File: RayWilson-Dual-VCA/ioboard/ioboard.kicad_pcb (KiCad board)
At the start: 2 copper layers, 108 x 71.8 mm, 90 parts, among them IC1 TL074P, IC2 LM13700N, Q1 2N3904, Q2 2N3906, Q3 2N3904, Q4 2N3906

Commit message: Update ioboard
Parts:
- removed @HOLE0, @HOLE1, @HOLE10, @HOLE2, @HOLE3, @HOLE4, @HOLE5, @HOLE6, @HOLE7, @HOLE8, @HOLE9: , 
- AUDIO_IN_1, AUDIO_IN_2, AUDIO_OUT_1, AUDIO_OUT_2, CV1_1, CV1_2, CV2_1, CV2_2: value PJ301BMPJ301BM -> AudioJack2_SwitchT; footprint ioboard:PJ301BM -> Connector_Audio:Jack_3.5mm_QingPu_WQP-PJ398SM_Vertical_CircularHoles
- JP1, JP2, JP3, JP4: value (none) -> PINHD-1X6
- JP5, JP6: value (none) -> PINHD-1X4
- PWR0: value (none) -> ML10
- S1, S2: value (none) -> M9040P
- moved CV2_2 6.49 mm to (163.1, 126.8), turned to 0 degrees
- moved CV1_2 6.48 mm to (194.8, 126.8), turned to 0 degrees
- moved AUDIO_IN_2 6.47 mm to (113.6, 126.8), turned to 0 degrees
- moved CV1_1 6.47 mm to (194.8, 119.4), turned to 180 degrees
- moved CV2_1 6.47 mm to (163.1, 119.4), turned to 180 degrees
- moved AUDIO_OUT_2 6.46 mm to (100.9, 126.8), turned to 0 degrees
- moved AUDIO_OUT_1 6.46 mm to (100.9, 119.4), turned to 180 degrees
- moved AUDIO_IN_1 6.45 mm to (113.6, 119.4), turned to 180 degrees
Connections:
- net AI1_M renamed /AI1_M
- net AI2_M renamed /AI2_M
- net AO1_M renamed /AO1_M
- net AO2_M renamed /AO2_M
- net CV1_IO renamed /CV1_IO
- net CV1_M renamed /CV1_M
- net CV2_IO renamed /CV2_IO
- net CV2_M renamed /CV2_M
- net IO_CV1 renamed Net-(CV_ATTN_1-Pad1)
- net IO_CV2 renamed Net-(CV_ATTN_2-Pad1)
- net SWA1_IO renamed /SWA1_IO
- net SWA1_M renamed /SWA1_M
- net SWA2_IO renamed /SWA2_IO
- net SWA2_M renamed /SWA2_M
- net SWB1_IO renamed /SWB1_IO
- net SWB1_M renamed /SWB1_M
- net SWB2_IO renamed /SWB2_IO
- net SWB2_M renamed /SWB2_M
- net SWC1_IO renamed /SWC1_IO
- net SWC1_M renamed /SWC1_M
- net SWC2_IO renamed /SWC2_IO
- net SWC2_M renamed /SWC2_M
- CV_ATTN_1 pad 2: N$41 -> Net-(CV1_1-PadT)
- CV_ATTN_2 pad 2: N$46 -> Net-(CV1_2-PadT)
- IC2 pad 15: (no net) -> unconnected-(IC2-Pad15)
- IC2 pad 2: (no net) -> unconnected-(IC2-Pad2)
- JP1 pad 2: AI2_IO -> /AI2_IO
- JP1 pad 6: AO2_IO -> /AO2_IO
- JP2 pad 2: AI1_IO -> /AI1_IO
- JP2 pad 6: AO1_IO -> /AO1_IO
- R1 pad S@1: (no net) -> unconnected-(R1-PadS@1)
- R16 pad 1: N$12 -> Net-(CV2_1-PadT)
- R2 pad S@1: (no net) -> unconnected-(R2-PadS@1)
- R3 pad S@1: (no net) -> unconnected-(R3-PadS@1)
- R36 pad 1: N$48 -> Net-(CV2_2-PadT)
- R4 pad S@1: (no net) -> unconnected-(R4-PadS@1)
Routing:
- net /AO1_IO: track 0.00 -> 30.6 mm
- net /AO2_IO: track 0.00 -> 30.2 mm
- net N$46: track 29.1 -> 0.00 mm
- net N$41: track 29.1 -> 0.00 mm
- net /AI2_IO: track 0.00 -> 28.7 mm
- net AI2_IO: track 27.5 -> 0.00 mm
- net /AI1_IO: track 0.00 -> 26.3 mm
- net Net-(CV1_2-PadT): track 0.00 -> 24.3 mm
- net Net-(CV1_1-PadT): track 0.00 -> 24.3 mm
- net AO1_IO: track 23.7 -> 0.00 mm
- net AO2_IO: track 22.9 -> 0.00 mm
- net AI1_IO: track 19.5 -> 0.00 mm
- net N$12: track 15.7 -> 0.00 mm
- net N$48: track 14.7 -> 0.00 mm
- net Net-(CV2_1-PadT): track 0.00 -> 9.88 mm
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
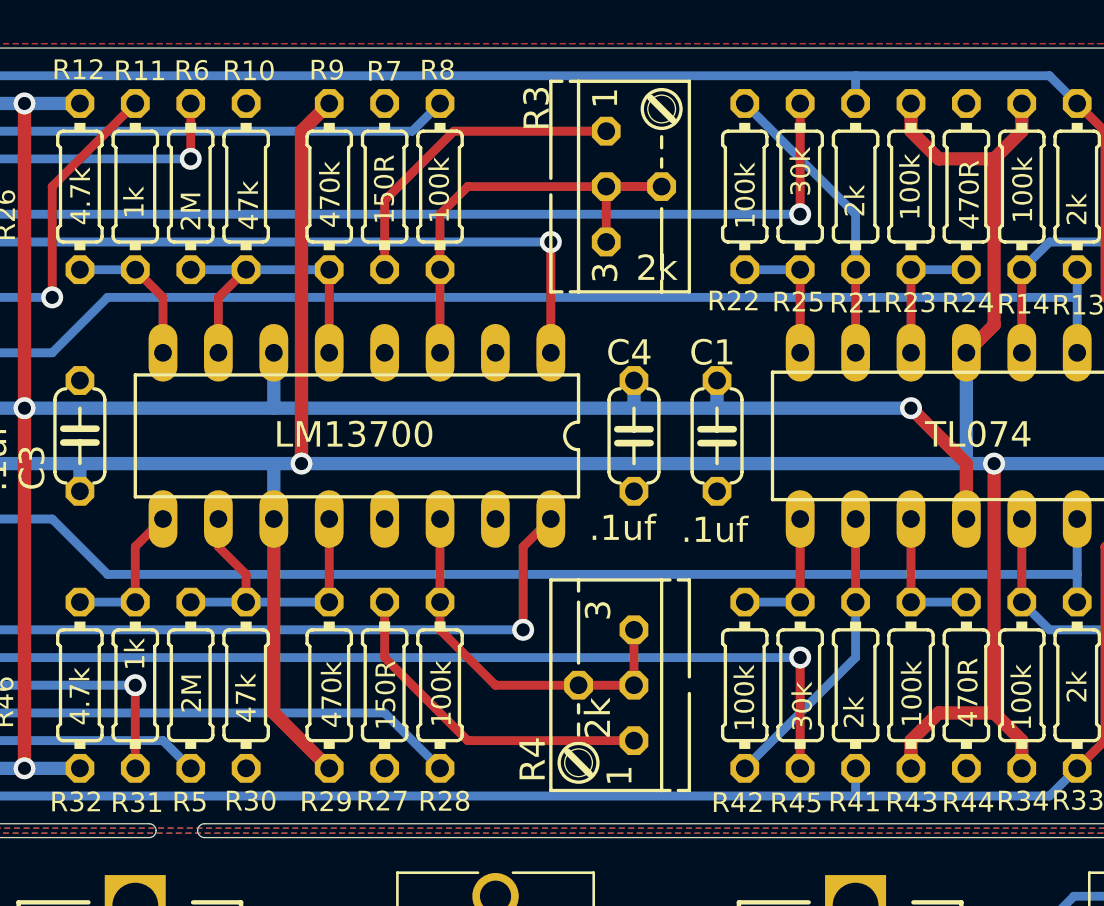
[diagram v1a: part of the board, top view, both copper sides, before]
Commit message: Change LM13700 to be SMD since that's the only part available
In both TME and LCSC.
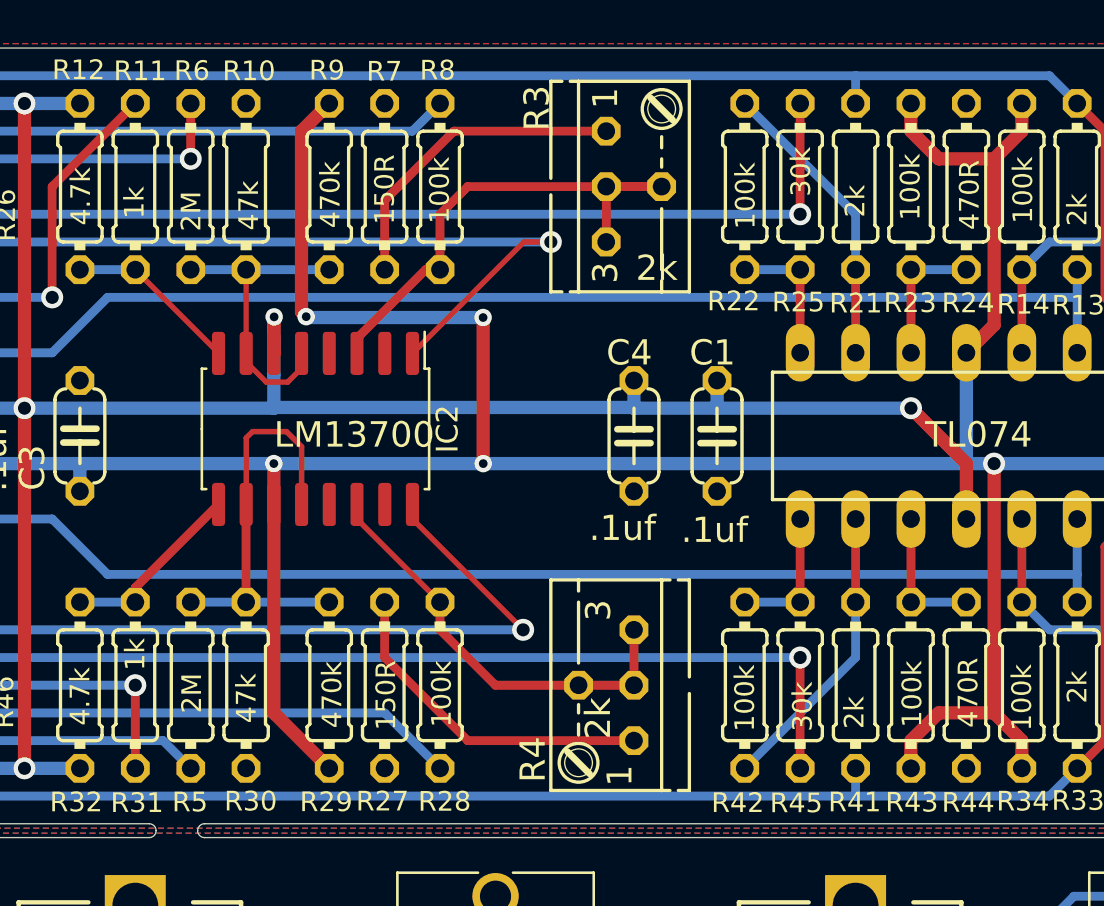
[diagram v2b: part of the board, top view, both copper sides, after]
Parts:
- IC2: footprint ioboard:DIL16 -> Package_SO:SO-16_5.3x10.2mm_P1.27mm
- moved IC2 1.93 mm to (154.9, 86.6), turned to -90 degrees
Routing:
- net +12V: track 275.8 -> 283.9 mm, vias 2 -> 5
- net Net-(IC2-Pad10): track 14.5 -> 19.5 mm
- net /SWB1_M: track 48.3 -> 51.6 mm
- net -12V: track 212.1 -> 215.4 mm, vias 5 -> 6
- net /SWB2_M: track 47.5 -> 49.8 mm
- net Net-(IC2-Pad14): track 17.6 -> 19.8 mm
- net Net-(IC2-Pad3): track 22.1 -> 24.1 mm
- net Net-(IC2-Pad9): track 6.88 -> 8.60 mm
- net Net-(IC2-Pad8): track 6.88 -> 7.96 mm

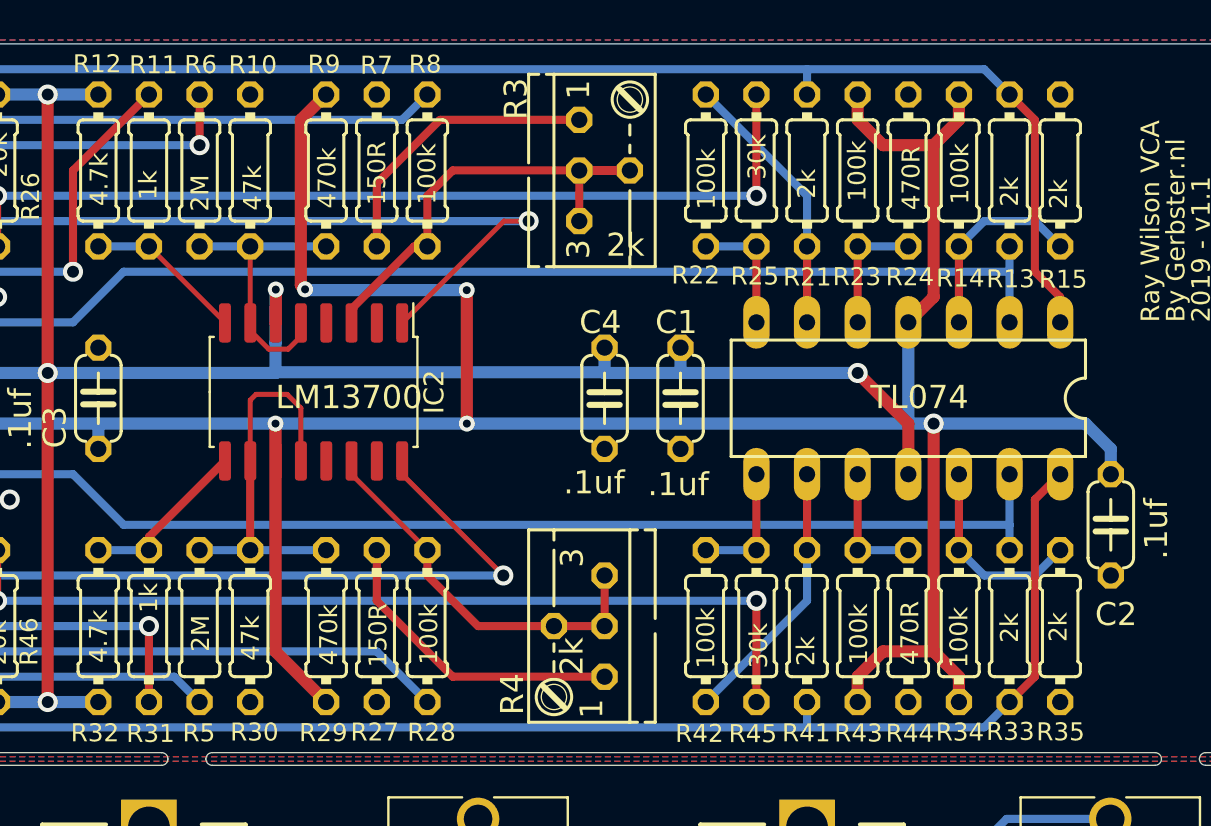
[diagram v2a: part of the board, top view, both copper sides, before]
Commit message: Replace TL047P with SMD
Since that's the only package available from LCSC.
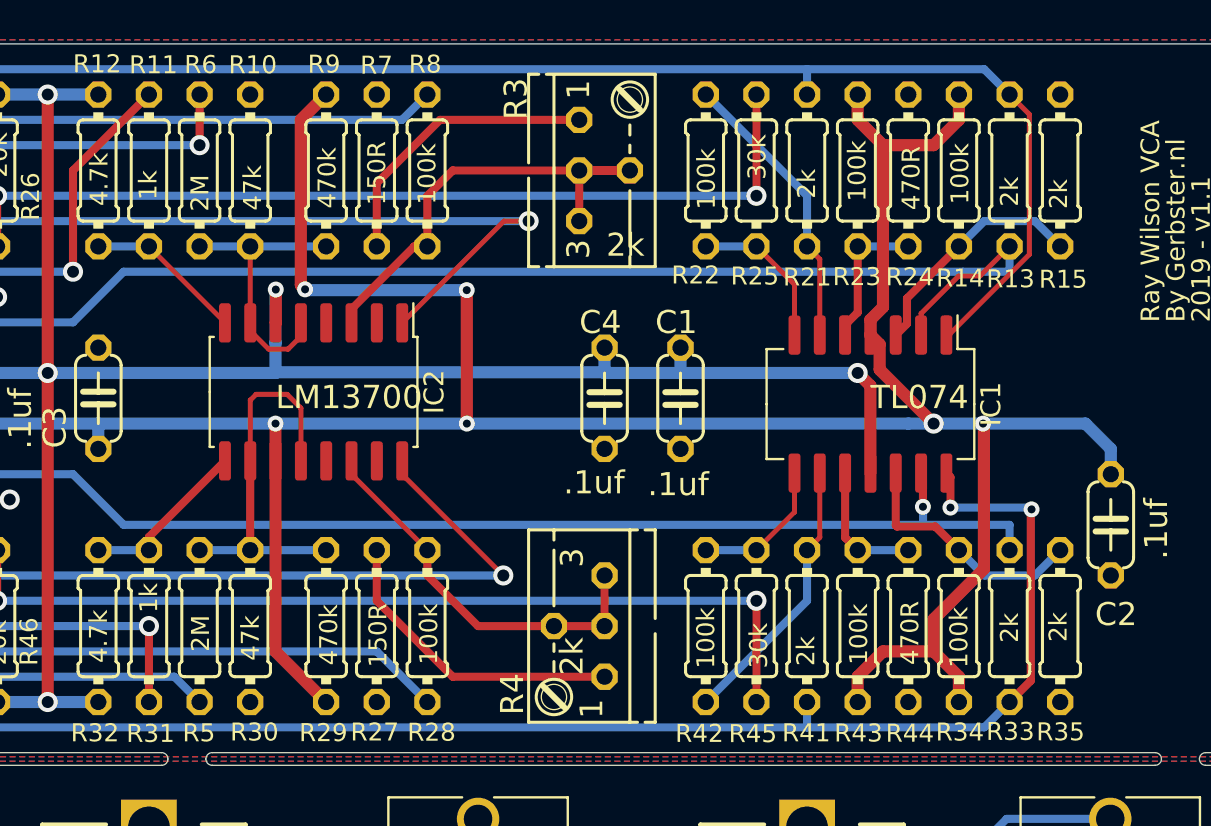
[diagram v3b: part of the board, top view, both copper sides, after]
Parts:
- IC1: footprint ioboard:DIL14 -> Package_SO:SO-14_5.3x10.2mm_P1.27mm
- moved IC1 1.92 mm to (182.8, 87.2), turned to -90 degrees
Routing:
- net /CV1_M: track 59.5 -> 63.8 mm
- net Net-(IC1-Pad14): track 101.7 -> 105.3 mm, vias 0 -> 2
- net Net-(IC1-Pad12): track 9.94 -> 12.4 mm
- net +12V: track 283.9 -> 286.0 mm, vias 5 -> 6
- net Net-(IC1-Pad3): track 9.94 -> 11.9 mm
- net Net-(IC1-Pad1): track 92.2 -> 94.0 mm
- net Net-(IC1-Pad7): track 6.35 -> 7.78 mm
- net Net-(IC1-Pad6): track 13.5 -> 14.4 mm
- net Net-(IC1-Pad5): track 6.35 -> 7.25 mm
- net Net-(IC1-Pad8): track 6.35 -> 7.20 mm
- net -12V: track 215.4 -> 214.6 mm
- net /CV2_M: track 59.5 -> 59.6 mm, vias 0 -> 1

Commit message: Align potentiometer packages to standard 3-pin 0.1"
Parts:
- R1, R2, R3, R4: footprint ioboard:S64YW -> Potentiometer_THT:Potentiometer_Bourns_3296W_Vertical
- moved R2 2.94 mm to (123.7, 72.9), turned to 180 degrees
- moved R1 2.94 mm to (123.7, 99.5), turned to 180 degrees
- moved R4 2.88 mm to (169.4, 95.7), turned to 90 degrees
- moved R3 2.81 mm to (168.1, 77.9), turned to -90 degrees
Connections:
- R5 pad 1: Net-(R1-PadS) -> Net-(R1-Pad2)
- R6 pad 1: Net-(R2-PadS) -> Net-(R2-Pad2)
- R7 pad 2: Net-(R3-PadA) -> Net-(R3-Pad3)
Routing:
- net Net-(R2-PadS): track 27.9 -> 0.00 mm, vias 1 -> 0
- net Net-(R2-Pad2): track 0.00 -> 27.9 mm, vias 0 -> 1
- net Net-(R1-PadS): track 25.9 -> 0.00 mm
- net Net-(R1-Pad2): track 0.00 -> 25.9 mm
- net Net-(R3-PadA): track 14.7 -> 0.00 mm
- net Net-(R3-Pad3): track 0.00 -> 14.7 mm
- net Net-(IC2-Pad3): track 24.1 -> 19.0 mm

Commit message: Align footprints to actual shapes
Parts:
- IC1: footprint Package_SO:SO-14_5.3x10.2mm_P1.27mm -> Package_SO:SO-14_3.9x8.65mm_P1.27mm
- IC2: footprint Package_SO:SO-16_5.3x10.2mm_P1.27mm -> Package_SO:SOIC-16_3.9x9.9mm_P1.27mm
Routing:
- net -12V: track 214.6 -> 213.6 mm
- net Net-(IC2-Pad5): track 14.4 -> 15.3 mm
- net +12V: track 286.0 -> 285.4 mm

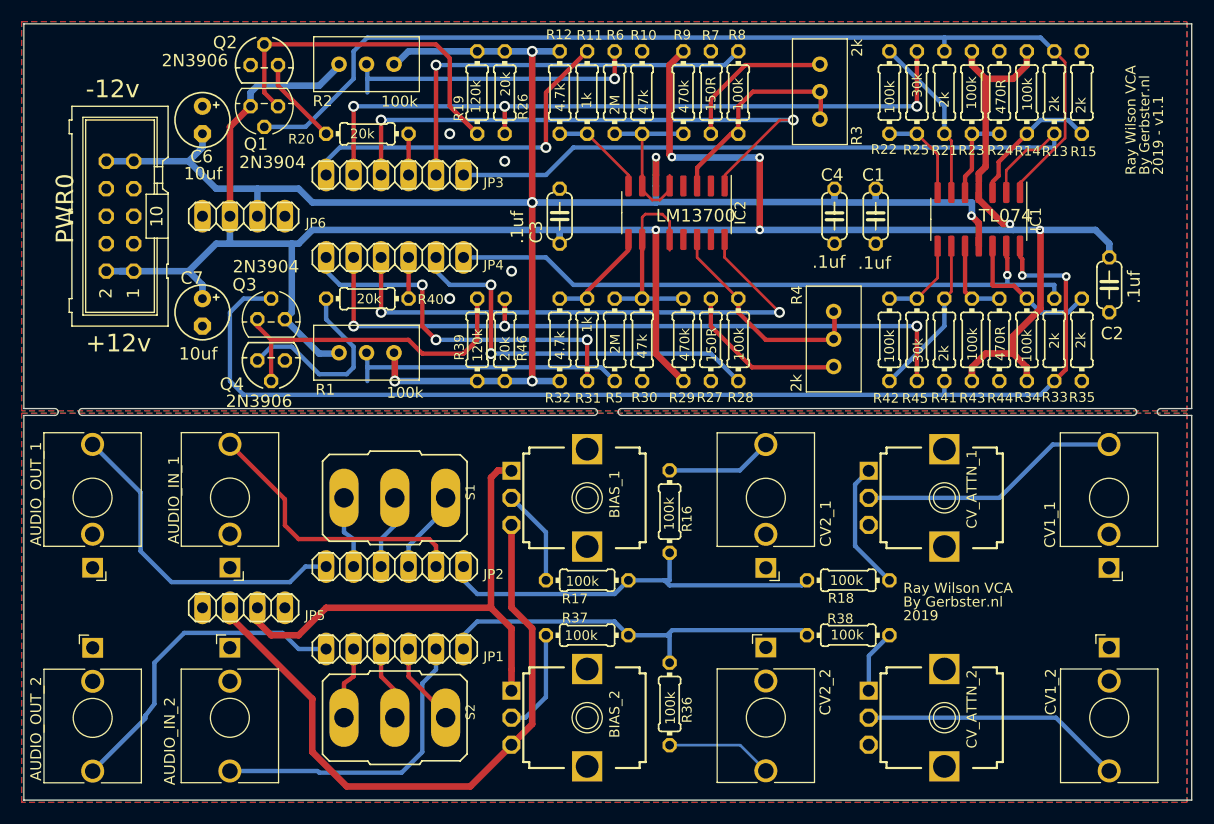
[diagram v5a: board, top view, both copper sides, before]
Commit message: Split up into separate main and io boards, update power silkscreen
Power connector silkscreen was updated to make it more obvious that the
connector is to be mounted on the backside, in the same orientation as
front silk screen.
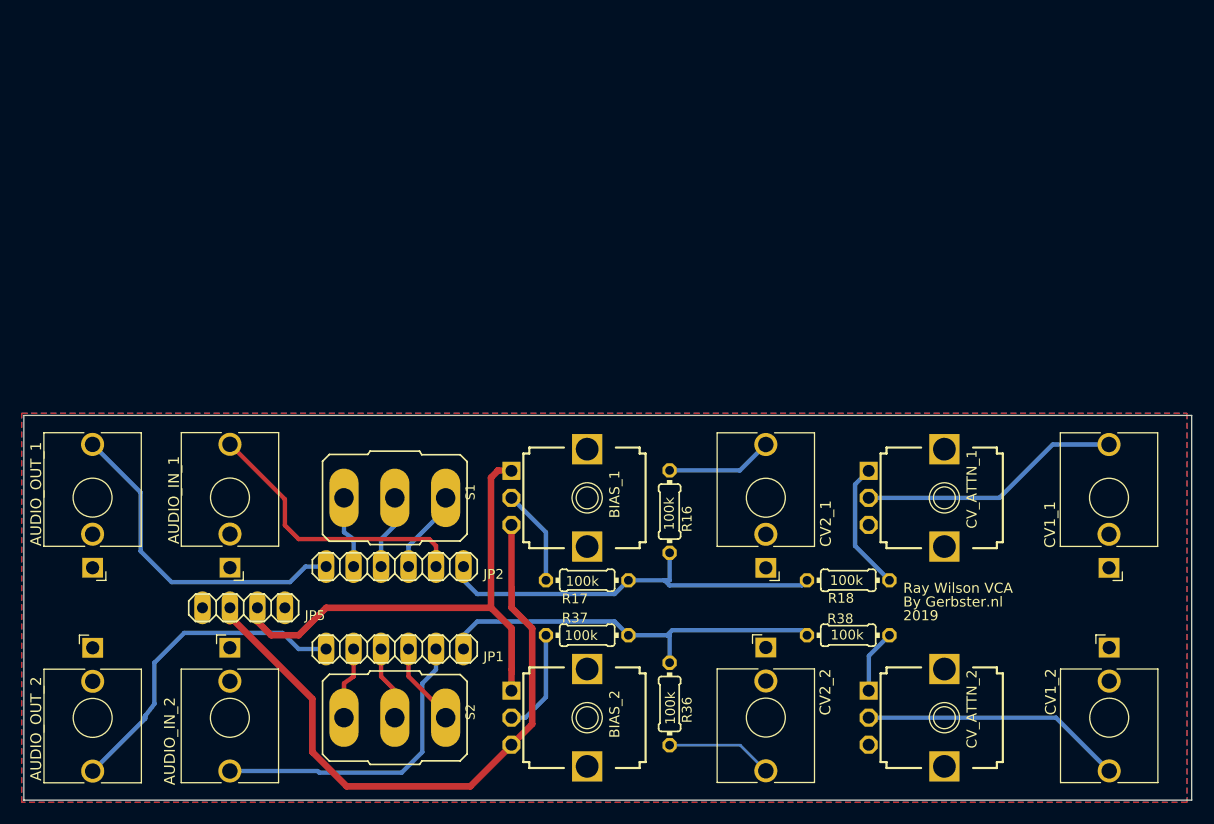
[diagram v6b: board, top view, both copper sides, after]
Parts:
- removed C1, C2, C3, C4: .1uf, ioboard:C050-024X044
- removed C6, C7: 10uf, ioboard:E2,5-5
- removed IC1: TL074P, Package_SO:SO-14_3.9x8.65mm_P1.27mm
- removed IC2: LM13700N, Package_SO:SOIC-16_3.9x9.9mm_P1.27mm
- removed JP3, JP4: PINHD-1X6, ioboard:1X06
- removed JP6: PINHD-1X4, ioboard:1X04
- removed PWR0: ML10, ioboard:ML10
- removed Q1, Q3: 2N3904, ioboard:TO92
- removed Q2, Q4: 2N3906, ioboard:TO92
- removed R1, R2: 100k, Potentiometer_THT:Potentiometer_Bourns_3296W_Vertical
- removed R10, R30: 47k, ioboard:0204_7
- removed R11, R31: 1k, ioboard:0204_7
- removed R12, R32: 4.7k, ioboard:0204_7
- removed R13, R15, R21, R33, R35, R41: 2k, ioboard:0204_7
- removed R14, R22, R23, R28, R34, R42, R43, R8: 100k, ioboard:0204_7
- removed R19, R39: 120k, ioboard:0204_7
- removed R20, R26, R40, R46: 20k, ioboard:0204_7
- removed R24, R44: 470R, ioboard:0204_7
- removed R25, R45: 30k, ioboard:0204_7
- removed R27, R7: 150R, ioboard:0204_7
- removed R29, R9: 470k, ioboard:0204_7
- removed R3, R4: 2k, Potentiometer_THT:Potentiometer_Bourns_3296W_Vertical
- removed R5, R6: 2M, ioboard:0204_7
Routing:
- net +12V: track 285.4 -> 61.0 mm, vias 6 -> 0
- net -12V: track 213.6 -> 47.1 mm, vias 6 -> 0
- net Net-(IC1-Pad14): track 105.3 -> 0.00 mm, vias 2 -> 0
- net Net-(IC1-Pad1): track 94.0 -> 0.00 mm
- net /SWC2_M: track 66.0 -> 0.00 mm, vias 3 -> 0
- net /SWC1_M: track 66.0 -> 0.00 mm, vias 3 -> 0
- net /CV1_M: track 63.8 -> 0.00 mm
- net /CV2_M: track 59.6 -> 0.00 mm, vias 1 -> 0
- net /SWB1_M: track 51.6 -> 0.00 mm, vias 2 -> 0
- net /SWB2_M: track 49.8 -> 0.00 mm, vias 2 -> 0
- net /AI1_M: track 38.6 -> 0.00 mm, vias 1 -> 0
- net /AI2_M: track 37.1 -> 0.00 mm, vias 2 -> 0
- net /AO2_M: track 34.1 -> 0.00 mm, vias 3 -> 0
- net /AO1_M: track 32.6 -> 0.00 mm, vias 1 -> 0
- net Net-(Q1-Pad3): track 31.9 -> 0.00 mm
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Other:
- board size 108 x 71.8 mm -> 108 x 35.6 mm
- board text removed: "+12v"
- board text removed: "-12v"
- board text removed: "2019 - v1.1"
- board text removed: "LM13700"
- board text removed: "TL074"

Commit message: Saving latest changes
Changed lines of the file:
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@@
       (effects (font (size 0.937484 0.937484) (thickness 0.078516)) (justify right))
     )
-    (fp_text value "50k" (at -3.81 3.81 -90) (layer "F.Fab") hide
+    (fp_text value "50k" (at 1.2989 3.6461 -90) (layer "F.SilkS")
       (effects (font (size 1.1684 1.1684) (thickness 0.1016)) (justify left bottom))
     )
@@
       (effects (font (size 0.937484 0.937484) (thickness 0.078516)) (justify right))
     )
-    (fp_text value "100k" (at -3.81 3.81 -90) (layer "F.Fab") hide
+    (fp_text value "100k" (at 1.8789 3.1261 -90) (layer "F.SilkS")
       (effects (font (size 1.1684 1.1684) (thickness 0.1016)) (justify left bottom))
     )
@@
       (effects (font (size 0.937484 0.937484) (thickness 0.078516)) (justify right))
     )
-    (fp_text value "50k" (at -3.81 3.81 -90) (layer "F.Fab") hide
+    (fp_text value "50k" (at 1.0089 3.7761 -90) (layer "F.SilkS")
       (effects (font (size 1.1684 1.1684) (thickness 0.1016)) (justify left bottom))
     )
@@
       (effects (font (size 0.937484 0.937484) (thickness 0.078516)) (justify right))
     )
-    (fp_text value "100k" (at -3.81 3.81 -90) (layer "F.Fab") hide
+    (fp_text value "100k" (at 1.2989 3.5161 -90) (layer "F.SilkS")
       (effects (font (size 1.1684 1.1684) (thickness 0.1016)) (justify left bottom))
     )
